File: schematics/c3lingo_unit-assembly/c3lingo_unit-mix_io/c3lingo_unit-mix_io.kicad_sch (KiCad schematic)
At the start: 38 parts, among them J201 Stage Line-In, J202 Mix Line-Out, J203 PowerSupply, J204 Ch1, J205 Ch2, J206 Ch3, SW201 GND Lift, U201 LM833-N, U202 DRV135UA

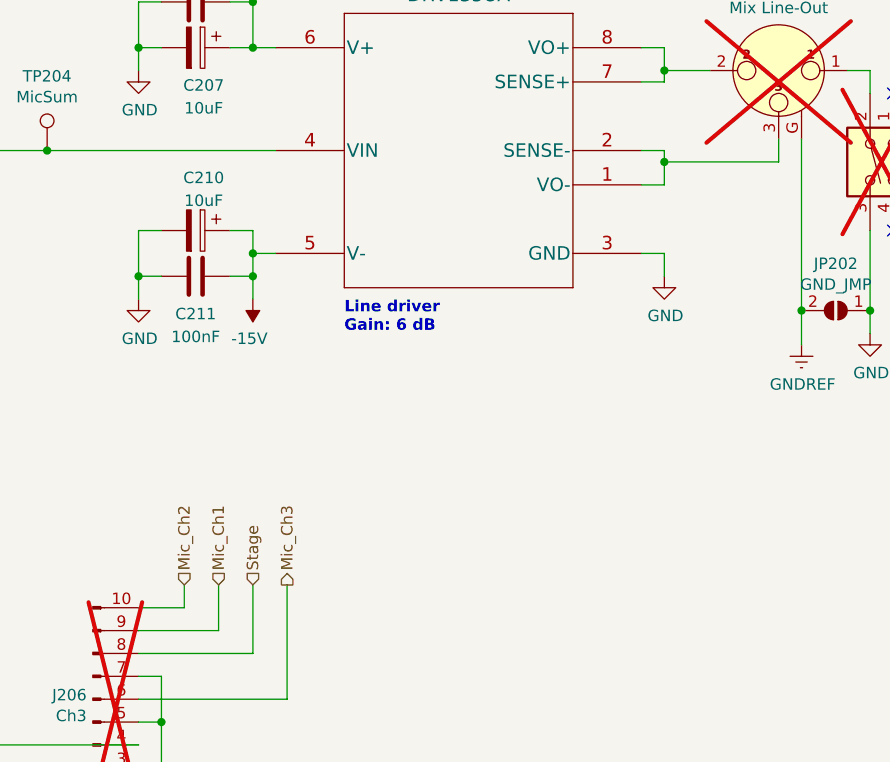
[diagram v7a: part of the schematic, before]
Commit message: Line I/O: Fix polarity of C210
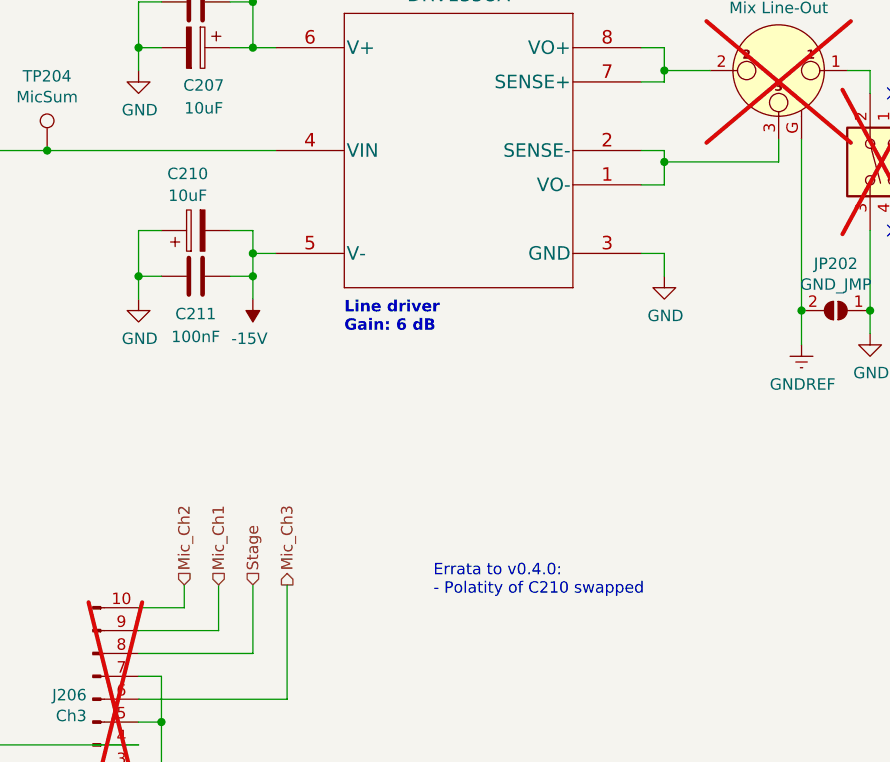
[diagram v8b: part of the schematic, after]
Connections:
- net -15V: now also C210.2; no longer C210.1
- net GND: now also C210.1; no longer C210.2
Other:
- note added: "Errata to v0.4.0: - Polatity of C210 swapped"
- moved on the sheet: C210
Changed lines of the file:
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@@
 	(title_block
 		(title "c3lingo interpeter unit -- main I/O")
-		(date "2025-08-26")
-		(rev "v0.4.0")
+		(date "2025-09-08")
+		(rev "v0.4.1")
 		(company "Jannik Beyerstedt (jtbx)")
-		(comment 1 "Prototype 3")
+		(comment 1 "Prototype 3 + Errata")
 	)
 	(text "Line driver\nGain: 6 dB"
@@
 		)
 	)
+	(text "Errata to v0.4.0:\n- Polatity of C210 swapped"
+		(exclude_from_sim no)
+		(at 177.546 163.83 0)
+		(effects
+			(font
+				(size 1.27 1.27)
+			)
+			(justify left bottom)
+		)
+	)
 	(junction
 		(at 120.65 109.22)
@@
 	(symbol
 		(lib_id "Device:C_Polarized")
-		(at 151.13 123.19 270)
+		(at 151.13 123.19 90)
 		(unit 1)
 		(exclude_from_sim no)
@@
 		(fields_autoplaced yes)
 		(property "Reference" "C210"
-			(at 152.019 117.3312 90)
+			(at 150.241 116.8865 90)
 			(effects
 				(font
@@
 		)
 		(property "Value" "10uF"
-			(at 152.019 119.8681 90)
+			(at 150.241 119.3108 90)
 			(effects
 				(font
@@
 		)
 		(property "Footprint" "Capacitor_SMD:CP_Elec_4x5.4"
-			(at 147.32 124.1552 0)
+			(at 154.94 122.2248 0)
 			(effects
 				(font
